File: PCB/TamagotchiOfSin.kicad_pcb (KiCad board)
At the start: 2 copper layers, 87.6 x 60.3 mm, 18 parts, among them SW1 SW_Push, SW2 SW_Push, SW3 SW_Push, U2 HS96L03W2C03, U3 DFR0299, U4 XIAO-ESP32-C3-SMD

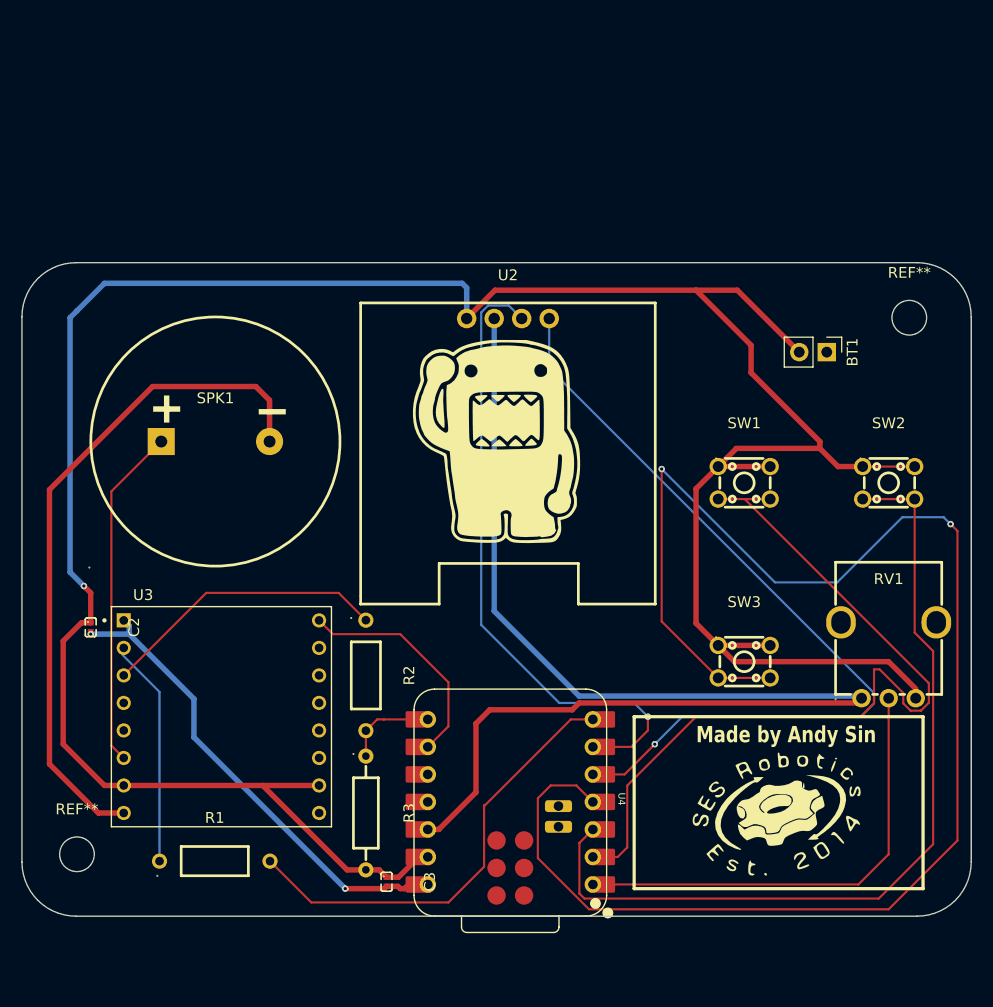
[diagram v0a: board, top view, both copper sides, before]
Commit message: updated cad, pcb, not code yet
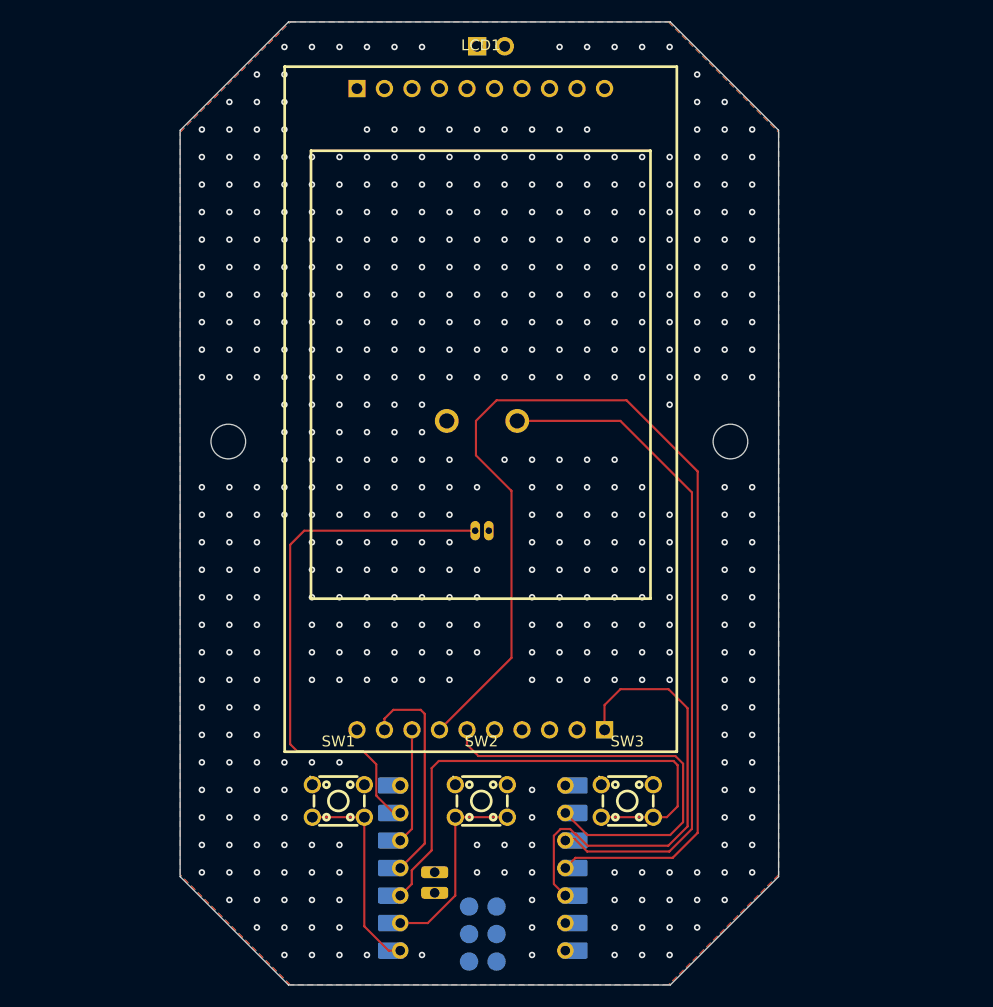
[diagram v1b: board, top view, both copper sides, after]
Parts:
- removed C2, C3: 10µF, easyeda2kicad:C0402
- removed the G*** at (134.6, 103.5)
- removed the G*** at (108.6, 69.2)
- removed R1, R2: 1k, easyeda2kicad:RES-TH_BD2.7-L6.2-P10.20-D0.4
- removed R3: 2k, easyeda2kicad:RES-TH_BD2.3-L6.5-P10.50-D0.5
- removed RV1: 10k, easyeda2kicad:RES-ADJ-TH_RK09D1130C3C
- removed SPK1: GSPK2307P-8R1W, easyeda2kicad:SPK-TH_BD23.0-P10.00-D0.8-L-RD
- removed U2: HS96L03W2C03, easyeda2kicad:OLED-TH_L27.8-W27.2-P2.54_C9900033791
- removed U3: DFR0299, DFR0299:MODULE_DFR0299
- added BUZZER1: 1207-P6.5MM, easyeda2kicad:BUZ-TH_BD12.5-P6.50-D1.4, B.Cu at (107.2, 67.3)
- added G***: LOGO, LOGO, B.Cu at (108.0, 51.4)
- added G***: LOGO, LOGO, B.Cu at (109.4, 86.5)
- added LCD1: HS20S010B, easyeda2kicad:LCD-TH_HS20S010B, F.Cu at (107.1, 66.2)
- added MOT1: LCM1027A2445F, easyeda2kicad:VIBRATING-MOTOR-SMD_WELDING, B.Cu at (107.2, 77.4)
- BT1, U4: moved to B.Cu
- moved SW2 47.7 mm to (107.2, 102.4)
- moved SW1 47.6 mm to (94.0, 102.4)
- moved BT1 42.9 mm to (106.8, 32.7)
- moved REF** 40.6 mm to (83.8, 69.2)
- moved REF** 20.1 mm to (130.2, 69.2)
- moved SW3 16.8 mm to (120.7, 102.4)
- moved U4 6.61 mm to (107.3, 108.6)
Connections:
- SW1 pad 2: Net-(U4-GPIO3_A1_D1) -> Net-(U4-GPIO2_A0_D0)
- SW2 pad 2: Net-(U4-GPIO4_A2_D2) -> Net-(U4-GPIO3_A1_D1)
- SW3 pad 2: Net-(U4-GPIO5_A3_D3) -> Net-(U4-GPIO4_A2_D2)
- U4 pad 10: unconnected-(U4-GPIO9_D9_MISO-Pad10)_1 -> Net-(BUZZER1-+)
- U4 pad 11: unconnected-(U4-GPIO10_D10_MOSI-Pad11) -> Net-(U4-GPIO10_D10_MOSI)
- U4 pad 7: Net-(U4-GPIO21_D6_TX) -> unconnected-(U4-GPIO21_D6_TX-Pad7)_1
- U4 pad 8: Net-(U4-GPIO20_D7_RX) -> unconnected-(U4-GPIO20_D7_RX-Pad8)_1
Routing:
- net GND: track 250.1 -> 0.07 mm, vias 1 -> 478
- net Net-(U4-GPIO5_A3_D3): track 144.5 -> 20.4 mm, vias 2 -> 0
- net Net-(U4-GPIO10_D10_MOSI): track 0.00 -> 103.5 mm
- net +3V3: track 113.0 -> 42.1 mm
- net Net-(U4-GPIO6_D4_SDA): track 76.6 -> 10.2 mm, vias 1 -> 0
- net Net-(BUZZER1-+): track 0.00 -> 63.0 mm
- net Net-(SPK1--): track 62.7 -> 0.00 mm
- net Net-(U4-GPIO3_A1_D1): track 76.5 -> 18.2 mm
- net +5V: track 45.5 -> 0.00 mm, vias 2 -> 0
- net Net-(U4-GPIO21_D6_TX): track 41.8 -> 0.00 mm
- net Net-(SPK1-+): track 31.6 -> 0.00 mm
- net Net-(U4-GPIO4_A2_D2): track 78.7 -> 47.4 mm
- net Net-(U3-TX): track 26.6 -> 0.00 mm
- net Net-(U4-GPIO2_A0_D0): track 42.9 -> 19.1 mm
- net Net-(U3-RX): track 20.5 -> 0.00 mm
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- added copper zone on B.Cu, net GND
- added copper zone on F.Cu, net GND
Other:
- board size 87.6 x 60.3 mm -> 55.2 x 88.9 mm
- board text added: "FOR HACKCLUB"
- board text added: "MADE BY ANDY SIN"
- board text removed: "Made by Andy Sin"
